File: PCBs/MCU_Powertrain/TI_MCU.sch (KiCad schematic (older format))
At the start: 29 parts

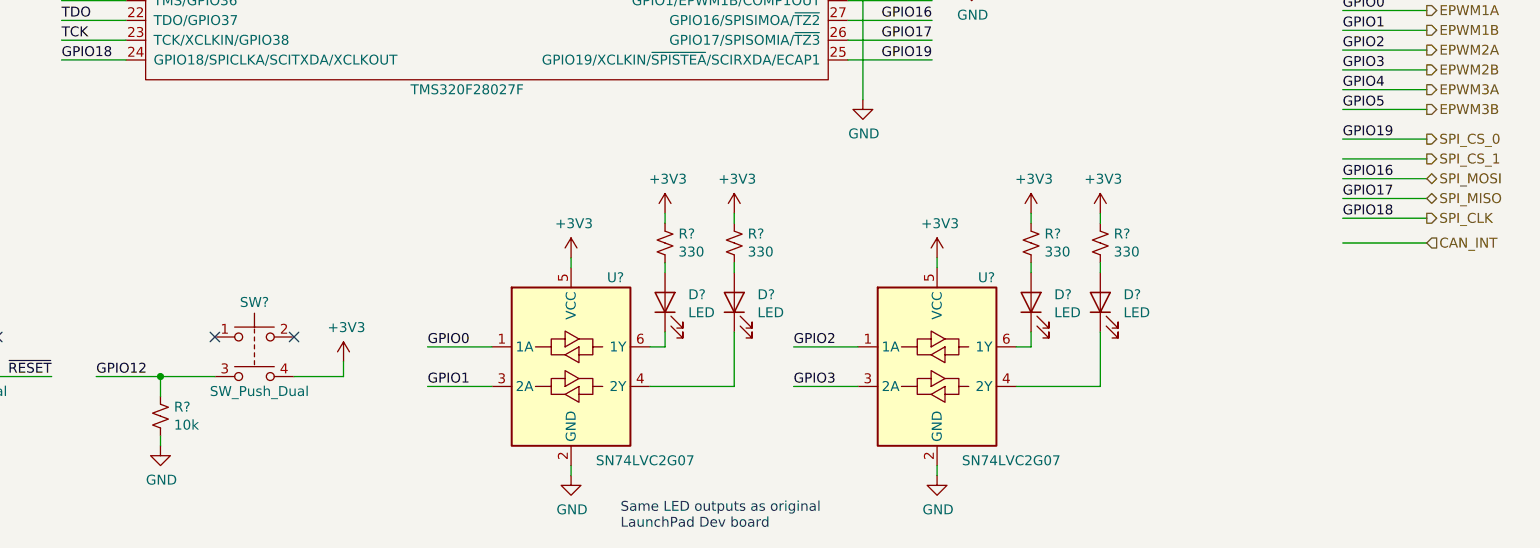
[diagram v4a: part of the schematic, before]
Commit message: TI_MCU Updates
- Connected GPIO12 to CAN_INT, made switch active low so that it can test the interrupt.
- Connected SPI CS_1 to GPIO32
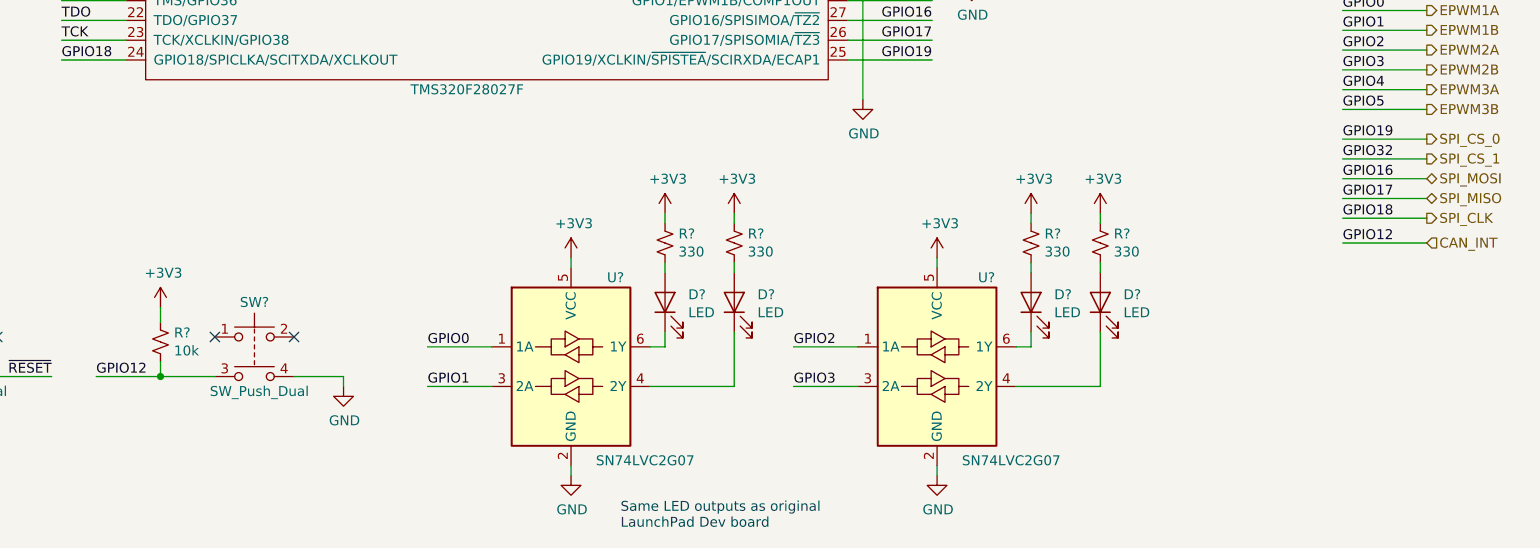
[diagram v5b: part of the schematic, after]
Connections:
- net GPIO32 is gone; now on net SPI_CS_1: U?.31 (GPIO32/SDAA/EPWMSYNCI/~ADCSOCAO~)
- net +3V3: now also R?.1; no longer SW?.4
- net CAN_INT: now also R?.2, SW?.3, U?.47 (GPIO12/~TZ1~/SCITXDA)
- net GND: now also SW?.4; no longer R?.2
- removed net GPIO12: R?.1, SW?.3, U?.47 (GPIO12/~TZ1~/SCITXDA)
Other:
- moved on the sheet: R?
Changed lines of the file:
@@
 Wire Wire Line
 	4575 5525 4825 5525
-Wire Wire Line
-	4825 5525 4825 5450
 $Comp
 L power:+3V3 #PWR?
 U 1 1 5E2D1E69
-P 4825 5450
-F 0 "#PWR?" H 4825 5300 50  0001 C CNN
-F 1 "+3V3" H 4840 5623 50  0000 C CNN
-F 2 "" H 4825 5450 50  0001 C CNN
-F 3 "" H 4825 5450 50  0001 C CNN
-	1    4825 5450
+P 3900 5175
+F 0 "#PWR?" H 3900 5025 50  0001 C CNN
+F 1 "+3V3" H 3915 5348 50  0000 C CNN
+F 2 "" H 3900 5175 50  0001 C CNN
+F 3 "" H 3900 5175 50  0001 C CNN
+	1    3900 5175
 	1    0    0    -1
 $EndComp
@@
 L Device:R_Small_US R?
 U 1 1 5E2D5182
-P 3900 5725
-F 0 "R?" H 3968 5771 50  0000 L CNN
-F 1 "10k" H 3968 5680 50  0000 L CNN
-F 2 "" H 3900 5725 50  0001 C CNN
-F 3 "~" H 3900 5725 50  0001 C CNN
-F 4 "" H 3900 5725 50  0001 C CNN "Digikey"
-	1    3900 5725
-	1    0    0    -1
-$EndComp
-Wire Wire Line
-	4175 5525 3900 5525
-Wire Wire Line
-	3900 5525 3900 5625
+P 3900 5350
+F 0 "R?" H 3968 5396 50  0000 L CNN
+F 1 "10k" H 3968 5305 50  0000 L CNN
+F 2 "" H 3900 5350 50  0001 C CNN
+F 3 "~" H 3900 5350 50  0001 C CNN
+F 4 "" H 3900 5350 50  0001 C CNN "Digikey"
+	1    3900 5350
+	1    0    0    -1
+$EndComp
 $Comp
 L power:GND #PWR?
 U 1 1 5E2D9CFB
-P 3900 5875
-F 0 "#PWR?" H 3900 5625 50  0001 C CNN
-F 1 "GND" H 3905 5702 50  0000 C CNN
-F 2 "" H 3900 5875 50  0001 C CNN
-F 3 "" H 3900 5875 50  0001 C CNN
-	1    3900 5875
-	1    0    0    -1
-$EndComp
-Wire Wire Line
-	3900 5825 3900 5875
+P 4825 5575
+F 0 "#PWR?" H 4825 5325 50  0001 C CNN
+F 1 "GND" H 4830 5402 50  0000 C CNN
+F 2 "" H 4825 5575 50  0001 C CNN
+F 3 "" H 4825 5575 50  0001 C CNN
+	1    4825 5575
+	1    0    0    -1
+$EndComp
+Wire Wire Line
+	4825 5525 4825 5575
 Text Label 3575 5525 0    50   ~ 0
 GPIO12
-Wire Wire Line
-	3575 5525 3900 5525
-Connection ~ 3900 5525
 Text Label 4250 1075 2    50   ~ 0
 TRST
@@
 Wire Wire Line
 	10300 4850 9875 4850
+Text Label 9875 4850 0    50   ~ 0
+GPIO12
+Wire Wire Line
+	3575 5525 3900 5525
+Wire Wire Line
+	3900 5450 3900 5525
+Connection ~ 3900 5525
+Wire Wire Line
+	3900 5525 4175 5525
+Wire Wire Line
+	3900 5250 3900 5175
+Text Label 9875 4425 0    50   ~ 0
+GPIO32
 $EndSCHEMATC

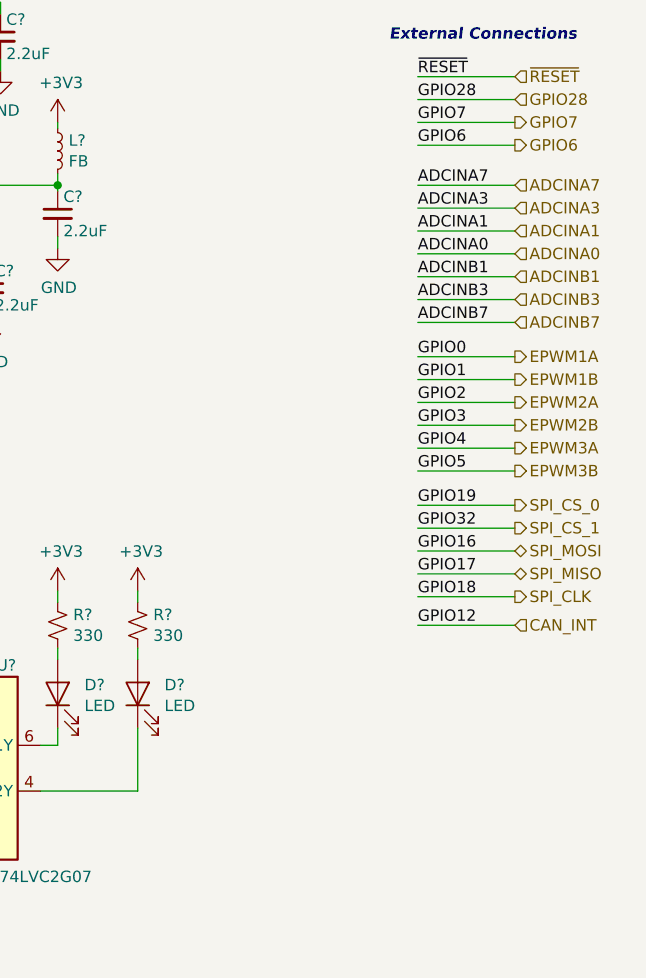
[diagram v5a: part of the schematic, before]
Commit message: Testpoints
- Added Testpoints everywhere!
- Schematic is "done" and any mistakes should be able to be corrected with small bodges later
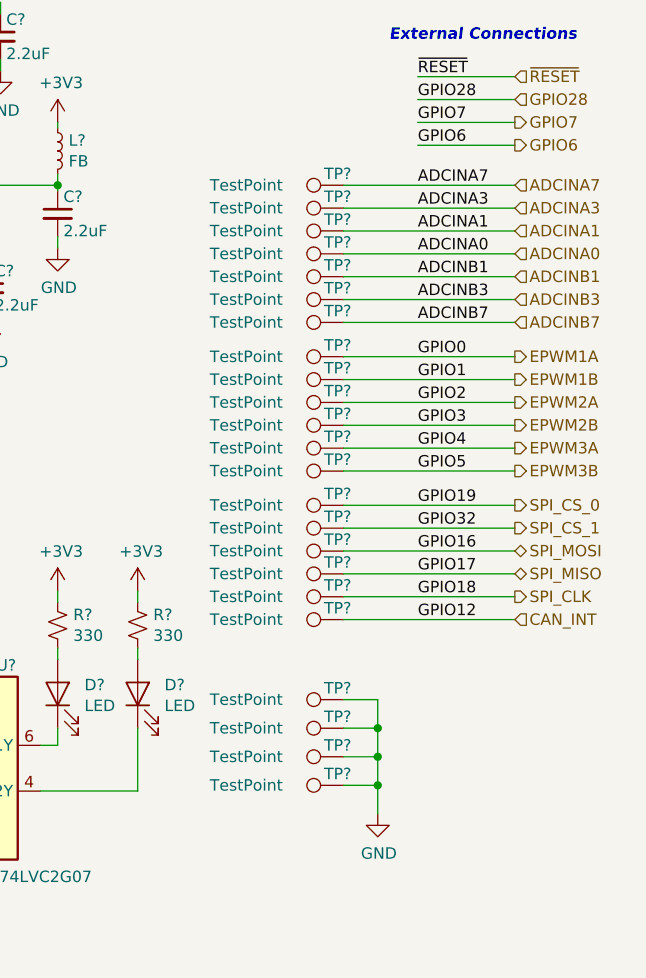
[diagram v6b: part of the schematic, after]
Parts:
- added TP? (x23): TestPoint, symbol Connector:TestPoint
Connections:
- net ADCINA0: now also TP?.1
- net ADCINA1: now also TP?.1
- net ADCINA3: now also TP?.1
- net ADCINA7: now also TP?.1
- net ADCINB1: now also TP?.1
- net ADCINB3: now also TP?.1
- net ADCINB7: now also TP?.1
- net CAN_INT: now also TP?.1
- net EPWM1A: now also TP?.1
- net EPWM1B: now also TP?.1
- net EPWM2A: now also TP?.1
- net EPWM2B: now also TP?.1
- net EPWM3A: now also TP?.1
- net EPWM3B: now also TP?.1
- net GND: now also TP?.1, TP?.1, TP?.1, TP?.1
- net SPI_CLK: now also TP?.1
- net SPI_CS_0: now also TP?.1
- net SPI_CS_1: now also TP?.1
- net SPI_MISO: now also TP?.1
- net SPI_MOSI: now also TP?.1

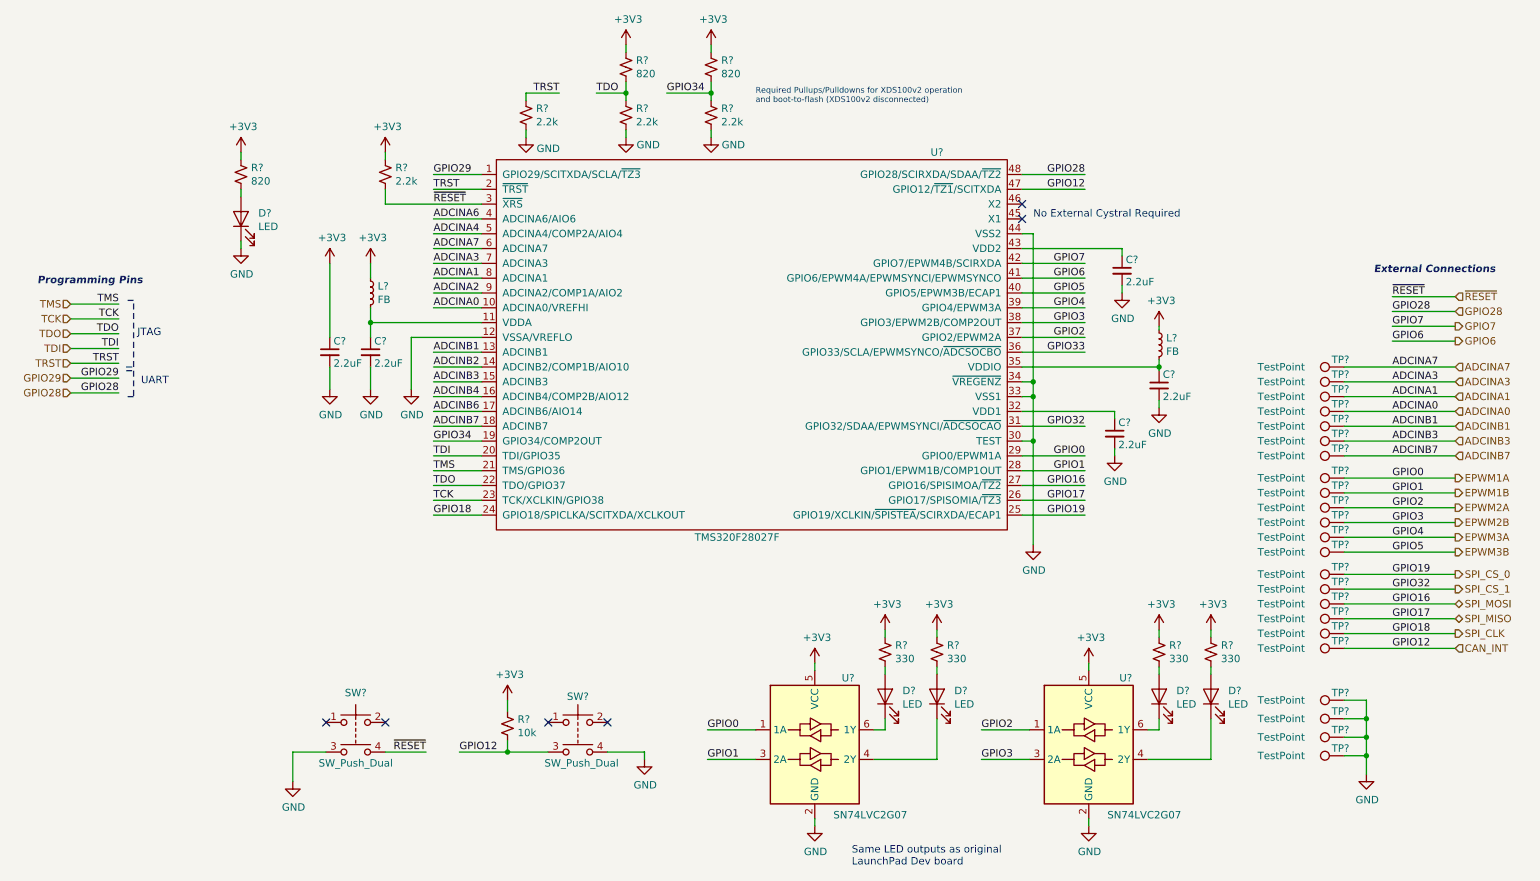
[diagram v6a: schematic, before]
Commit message: Completed BOM
- Added Digikey PNs to each component.
- Removed double 3V3 LED indicator
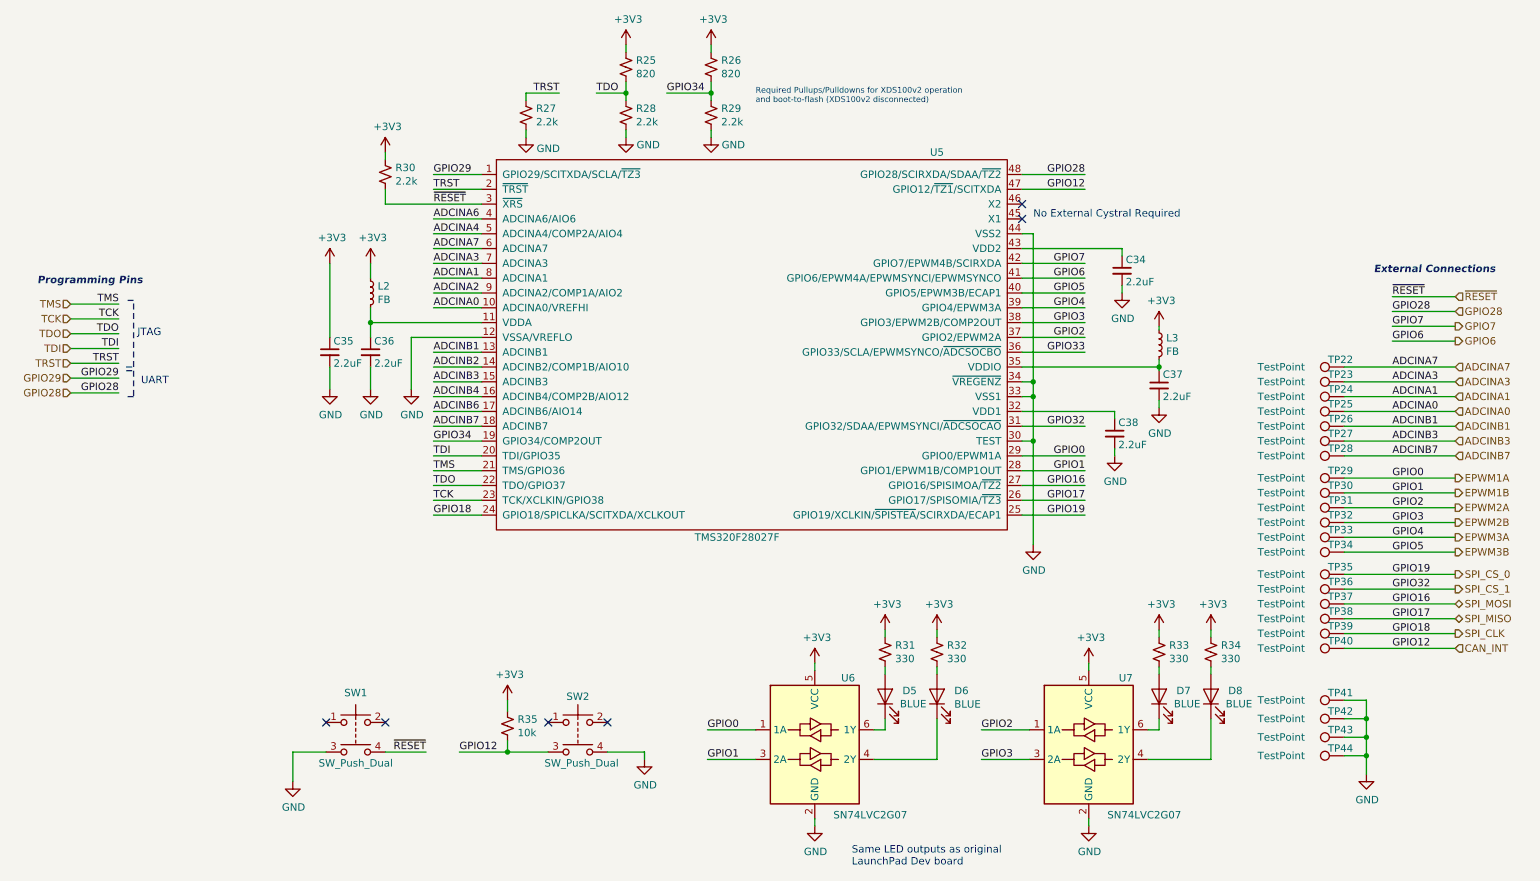
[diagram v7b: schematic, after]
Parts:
- removed D?: LED, symbol Device:LED
- removed R?: 820, symbol Device:R_Small_US
- removed TP? (x15): TestPoint, symbol Connector:TestPoint
- added TP23, TP24, TP25, TP26, TP27, TP28, TP31, TP32, TP33, TP34, TP36, TP37, TP38, TP39, TP40: TestPoint, symbol Connector:TestPoint
- C34, C35, C36, C37, C38: renamed from C?; Digikey (none) -> 1276-1763-1-ND
- D5, D6, D7, D8: renamed from D?; value LED -> BLUE; Digikey (none) -> 732-4982-1-ND
- L2: renamed from L?; footprint (none) -> Inductors_SMD:L_0805; Digikey (none) -> 240-2549-1-ND
- L3: renamed from L?; footprint (none) -> Inductors_SMD:L_0402; Digikey (none) -> 445-172882-1-ND
- R25, R26: renamed from R?; Digikey (none) -> 311-820ARCT-ND
- R27, R28, R29, R30: renamed from R?; Digikey (none) -> 541-4139-1-ND
- R31, R32, R33, R34: renamed from R?; Digikey (none) -> A129743CT-ND
- R35: renamed from R?; Digikey (none) -> 311-10.0KCRCT-ND
- SW1, SW2: renamed from SW?; Digikey (none) -> CKN9112CT-ND
- TP22: renamed from TP?; Digikey (none) -> 36-5117-ND
- TP29, TP30: renamed from TP?; Digikey (none) -> 36-5116-ND
- TP35: renamed from TP?; Digikey (none) -> 36-5119-ND
- TP41, TP42, TP43, TP44: renamed from TP?; Digikey (none) -> 36-5001-ND
- U5: renamed from U?; footprint (none) -> Housings_QFP:LQFP-48_7x7mm_Pitch0.5mm; Digikey (none) -> 296-36409-ND
- U6, U7: renamed from U?; Digikey (none) -> 296-13494-1-ND
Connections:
- net ADCINA0: now also TP25.1
- net ADCINA1: now also TP24.1
- net ADCINA3: now also TP23.1
- net ADCINB1: now also TP26.1
- net ADCINB3: now also TP27.1
- net ADCINB7: now also TP28.1
- net CAN_INT: now also TP40.1
- net EPWM2A: now also TP31.1
- net EPWM2B: now also TP32.1
- net EPWM3A: now also TP33.1
- net EPWM3B: now also TP34.1
- net SPI_CLK: now also TP39.1
- net SPI_CS_1: now also TP36.1
- net SPI_MISO: now also TP38.1
- net SPI_MOSI: now also TP37.1

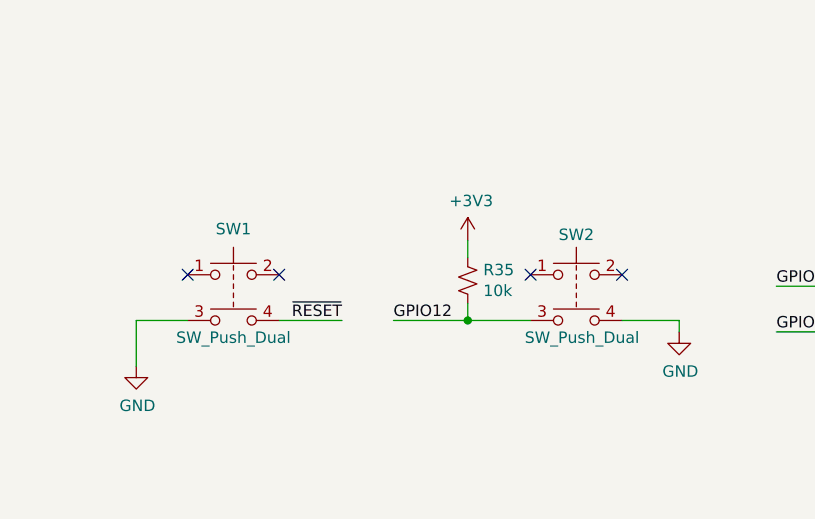
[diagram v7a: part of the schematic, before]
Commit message: Assigned Footprints
- All footprints assigned
- Created RA 3mm bullet fooprint, may need to adjust it later
- Fixed errors
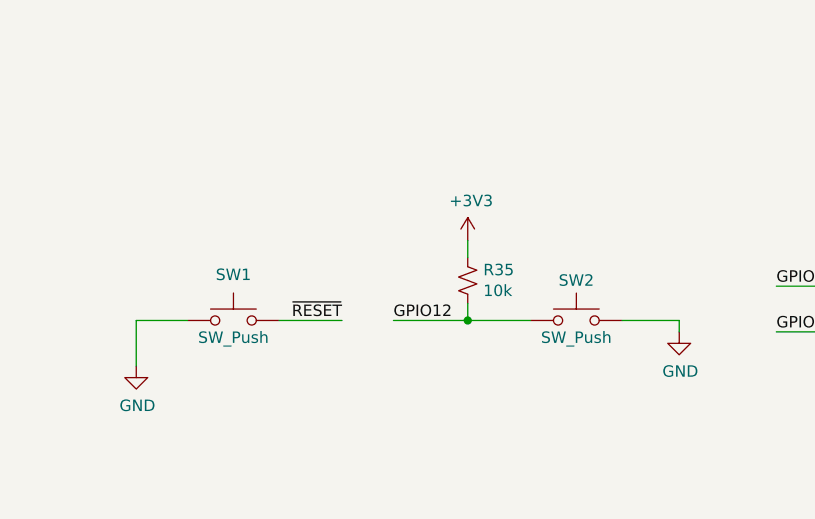
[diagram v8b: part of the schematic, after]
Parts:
- removed SW1, SW2: SW_Push_Dual, symbol Switch:SW_Push_Dual
- added SW1, SW2: SW_Push, Buttons_Switches_SMD:SW_SPST_EVQQ2, symbol Switch:SW_Push
- C34, C35, C36, C37, C38: footprint (none) -> Capacitors_SMD:C_0805
- D5, D6, D7, D8: footprint (none) -> LEDs:LED_0805
- R25, R26, R27, R28, R29, R30, R31, R32, R33, R34, R35: footprint (none) -> Resistors_SMD:R_0805
- TP22, TP23, TP24, TP25, TP26, TP27, TP28, TP29, TP30, TP31, TP32, TP33, TP34, TP35, TP36, TP37, TP38, TP39, TP40, TP41, TP42, TP43, TP44: footprint (none) -> Testpoints:TestPoint_Loop_D1.80mm_Drill1.0mm_Beaded
- U6, U7: footprint Package_SO:VSSOP-8_2.4x2.1mm_P0.5mm -> Housings_SSOP:VSSOP-8_2.4x2.1mm_Pitch0.5mm
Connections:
- net CAN_INT: now also SW2.1
- net GND: now also SW1.1, SW2.2
- net ~RESET~: now also SW1.2
- no-connect marks 6 -> 2
